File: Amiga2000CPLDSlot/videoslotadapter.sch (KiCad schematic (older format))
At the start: 13 parts, among them J1 Raspberry_Pi_2_3, J2 JTAG, U1 XC9572VQ44

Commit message: Amiga2000CPLDSlot v1.1
Made the following changes after some Discord chats:

* Added optional buttons 2 & 3
* Added an arrow to point to the rear of the Amiga
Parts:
- added JButton3, JButton4, JButton5, JButton6: Conn_01x02, Connector_PinHeader_2.54mm:PinHeader_1x02_P2.54mm_Horizontal, symbol Connector_Generic:Conn_01x02
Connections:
- net GND: now also JButton3.1 (Pin_1), JButton4.1 (Pin_1), JButton5.1 (Pin_1), JButton6.1 (Pin_1)
- net GPIO19: now also JButton3.2 (Pin_2), JButton4.2 (Pin_2)
- net GPIO26: now also JButton5.2 (Pin_2), JButton6.2 (Pin_2)
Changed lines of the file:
@@
 Text Label 8650 4550 2    50   ~ 0
 TMS
+$Comp
+L Connector_Generic:Conn_01x02 JButton6
+U 1 1 607564A8
+P 9850 9800
+F 0 "JButton6" V 9723 9880 50  0000 L CNN
+F 1 "Conn_01x02" V 9814 9880 50  0000 L CNN
+F 2 "Connector_PinHeader_2.54mm:PinHeader_1x02_P2.54mm_Horizontal" H 9850 9800 50  0001 C CNN
+F 3 "~" H 9850 9800 50  0001 C CNN
+	1    9850 9800
+	0    1    1    0
+$EndComp
+$Comp
+L power:GND #PWR0104
+U 1 1 607564AE
+P 9950 9400
+F 0 "#PWR0104" H 9950 9150 50  0001 C CNN
+F 1 "GND" V 9955 9272 50  0000 R CNN
+F 2 "" H 9950 9400 50  0001 C CNN
+F 3 "" H 9950 9400 50  0001 C CNN
+	1    9950 9400
+	0    -1   -1   0
+$EndComp
+Wire Wire Line
+	9850 9600 9850 9400
+Wire Wire Line
+	9850 9400 9950 9400
+Wire Wire Line
+	9750 9600 9750 9200
+$Comp
+L Connector_Generic:Conn_01x02 JButton5
+U 1 1 607564B7
+P 9050 9800
+F 0 "JButton5" V 8923 9880 50  0000 L CNN
+F 1 "Conn_01x02" V 9014 9880 50  0000 L CNN
+F 2 "Connector_PinHeader_2.54mm:PinHeader_1x02_P2.54mm_Horizontal" H 9050 9800 50  0001 C CNN
+F 3 "~" H 9050 9800 50  0001 C CNN
+	1    9050 9800
+	0    1    1    0
+$EndComp
+$Comp
+L power:GND #PWR0105
+U 1 1 607564BD
+P 9150 9450
+F 0 "#PWR0105" H 9150 9200 50  0001 C CNN
+F 1 "GND" V 9155 9322 50  0000 R CNN
+F 2 "" H 9150 9450 50  0001 C CNN
+F 3 "" H 9150 9450 50  0001 C CNN
+	1    9150 9450
+	0    -1   -1   0
+$EndComp
+Wire Wire Line
+	9050 9450 9150 9450
+Wire Wire Line
+	9050 9600 9050 9450
+Wire Wire Line
+	8950 9200 8950 9600
+Text Label 9700 9200 0    50   ~ 0
+GPIO26
+Wire Wire Line
+	8950 9200 9750 9200
+$Comp
+L Connector_Generic:Conn_01x02 JButton4
+U 1 1 6075F333
+P 8700 8650
+F 0 "JButton4" V 8573 8730 50  0000 L CNN
+F 1 "Conn_01x02" V 8664 8730 50  0000 L CNN
+F 2 "Connector_PinHeader_2.54mm:PinHeader_1x02_P2.54mm_Horizontal" H 8700 8650 50  0001 C CNN
+F 3 "~" H 8700 8650 50  0001 C CNN
+	1    8700 8650
+	0    1    1    0
+$EndComp
+$Comp
+L power:GND #PWR0106
+U 1 1 6075F339
+P 8800 8250
+F 0 "#PWR0106" H 8800 8000 50  0001 C CNN
+F 1 "GND" V 8805 8122 50  0000 R CNN
+F 2 "" H 8800 8250 50  0001 C CNN
+F 3 "" H 8800 8250 50  0001 C CNN
+	1    8800 8250
+	0    -1   -1   0
+$EndComp
+Wire Wire Line
+	8700 8450 8700 8250
+Wire Wire Line
+	8700 8250 8800 8250
+Wire Wire Line
+	8600 8450 8600 8050
+$Comp
+L Connector_Generic:Conn_01x02 JButton3
+U 1 1 6075F342
+P 7900 8650
+F 0 "JButton3" V 7773 8730 50  0000 L CNN
+F 1 "Conn_01x02" V 7864 8730 50  0000 L CNN
+F 2 "Connector_PinHeader_2.54mm:PinHeader_1x02_P2.54mm_Horizontal" H 7900 8650 50  0001 C CNN
+F 3 "~" H 7900 8650 50  0001 C CNN
+	1    7900 8650
+	0    1    1    0
+$EndComp
+$Comp
+L power:GND #PWR0107
+U 1 1 6075F348
+P 8000 8300
+F 0 "#PWR0107" H 8000 8050 50  0001 C CNN
+F 1 "GND" V 8005 8172 50  0000 R CNN
+F 2 "" H 8000 8300 50  0001 C CNN
+F 3 "" H 8000 8300 50  0001 C CNN
+	1    8000 8300
+	0    -1   -1   0
+$EndComp
+Wire Wire Line
+	7900 8300 8000 8300
+Wire Wire Line
+	7900 8450 7900 8300
+Wire Wire Line
+	7800 8050 7800 8450
+Text Label 8550 8050 0    50   ~ 0
+GPIO19
+Wire Wire Line
+	7800 8050 8600 8050
 $EndSCHEMATC

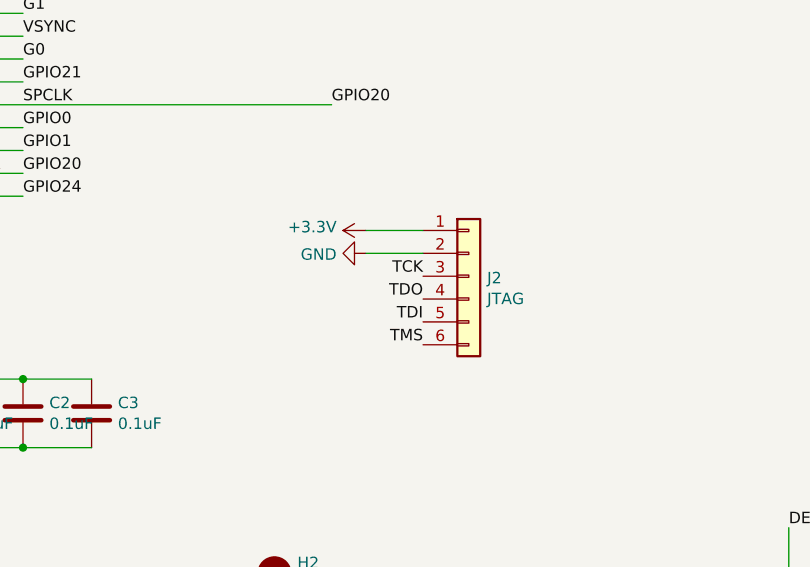
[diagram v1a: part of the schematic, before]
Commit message: Final tested release of Amiga 2000 CPLD edition
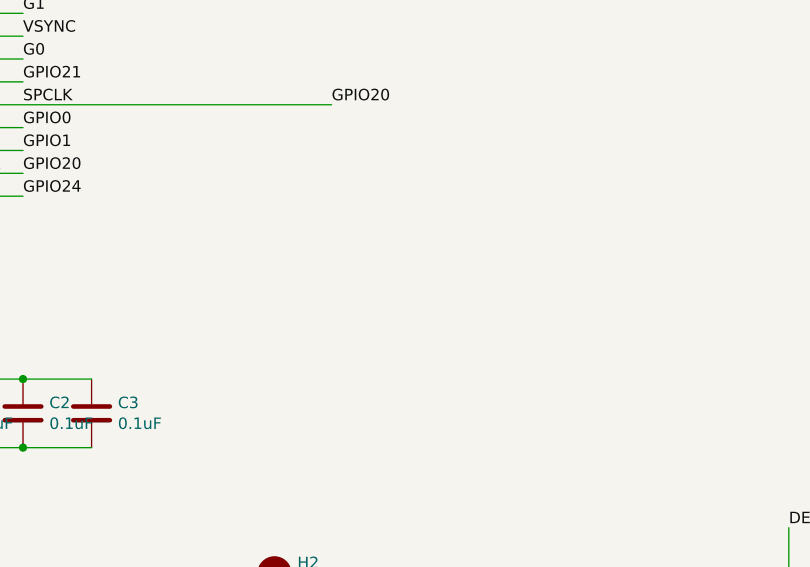
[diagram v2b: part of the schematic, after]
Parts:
- removed J2: JTAG, Connector_PinHeader_2.54mm:PinHeader_1x06_P2.54mm_Vertical, symbol Connector_Generic:Conn_01x06
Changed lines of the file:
@@
 	1    0    0    -1
 $EndComp
-$Comp
-L Connector_Generic:Conn_01x06 J2
-U 1 1 609EC0F8
-P 10700 4900
-F 0 "J2" H 10780 4892 50  0000 L CNN
-F 1 "JTAG" H 10780 4801 50  0000 L CNN
-F 2 "Connector_PinHeader_2.54mm:PinHeader_1x06_P2.54mm_Vertical" H 10700 4900 50  0001 C CNN
-F 3 "~" H 10700 4900 50  0001 C CNN
-	1    10700 4900
-	1    0    0    -1
-$EndComp
-$Comp
-L power:+3.3V #PWR0102
-U 1 1 609ED717
-P 10250 4700
-F 0 "#PWR0102" H 10250 4550 50  0001 C CNN
-F 1 "+3.3V" V 10265 4828 50  0000 L CNN
-F 2 "" H 10250 4700 50  0001 C CNN
-F 3 "" H 10250 4700 50  0001 C CNN
-	1    10250 4700
-	0    -1   -1   0
-$EndComp
-$Comp
-L power:GND #PWR0103
-U 1 1 609EE3AD
-P 10250 4800
-F 0 "#PWR0103" H 10250 4550 50  0001 C CNN
-F 1 "GND" V 10255 4672 50  0000 R CNN
-F 2 "" H 10250 4800 50  0001 C CNN
-F 3 "" H 10250 4800 50  0001 C CNN
-	1    10250 4800
-	0    1    1    0
-$EndComp
-Wire Wire Line
-	10250 4700 10500 4700
-Wire Wire Line
-	10500 4800 10250 4800
-Text Label 10500 4900 2    50   ~ 0
-TCK
-Text Label 10500 5000 2    50   ~ 0
-TDO
-Text Label 10500 5100 2    50   ~ 0
-TDI
-Text Label 10500 5200 2    50   ~ 0
-TMS
 Text Label 8650 4250 2    50   ~ 0
 TDI
